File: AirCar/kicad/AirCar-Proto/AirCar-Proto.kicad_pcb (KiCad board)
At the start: 2 copper layers, 76.2 x 55.9 mm, 16 parts, among them J1 Conn_01x05, J3 Conn_01x06, J4 PJ-102A, SW2 SW_SPDT, U1 Pico, U2 LM7805_TO220

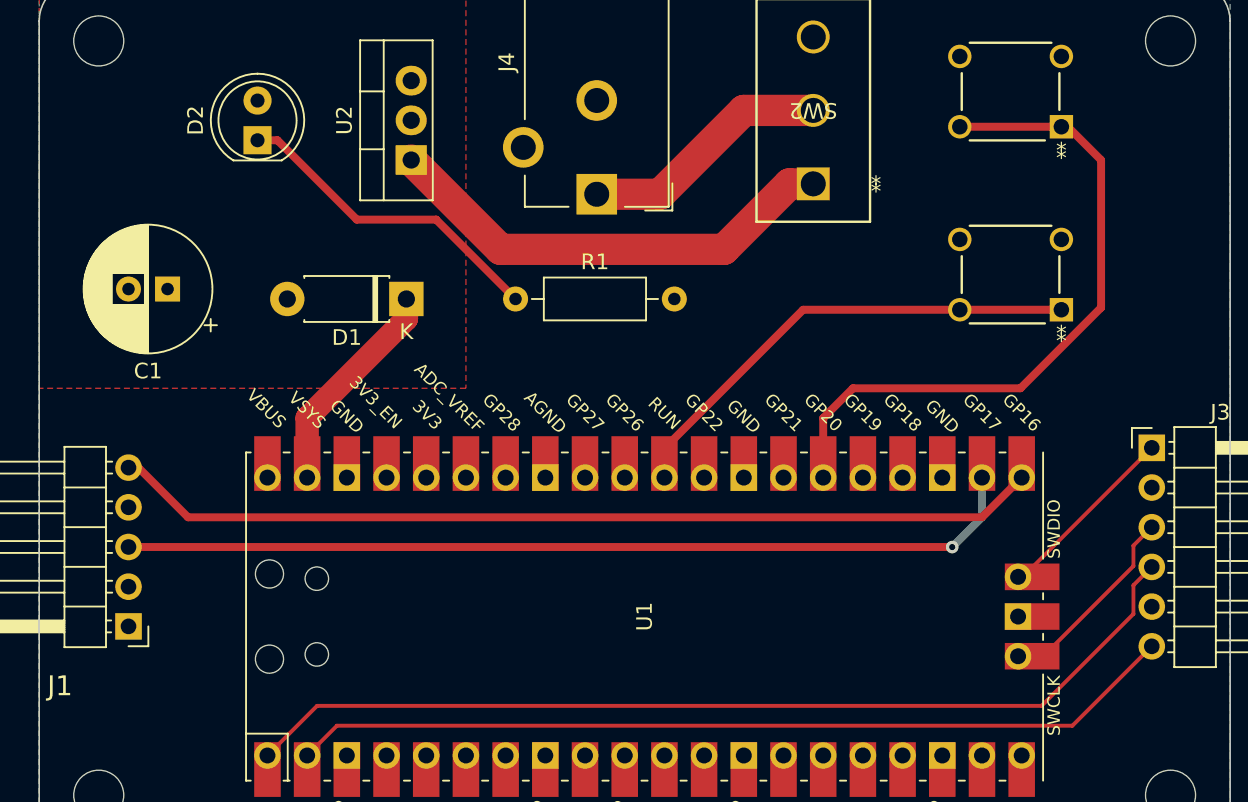
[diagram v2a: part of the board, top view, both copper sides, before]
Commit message: works w/ 3.3v encoder
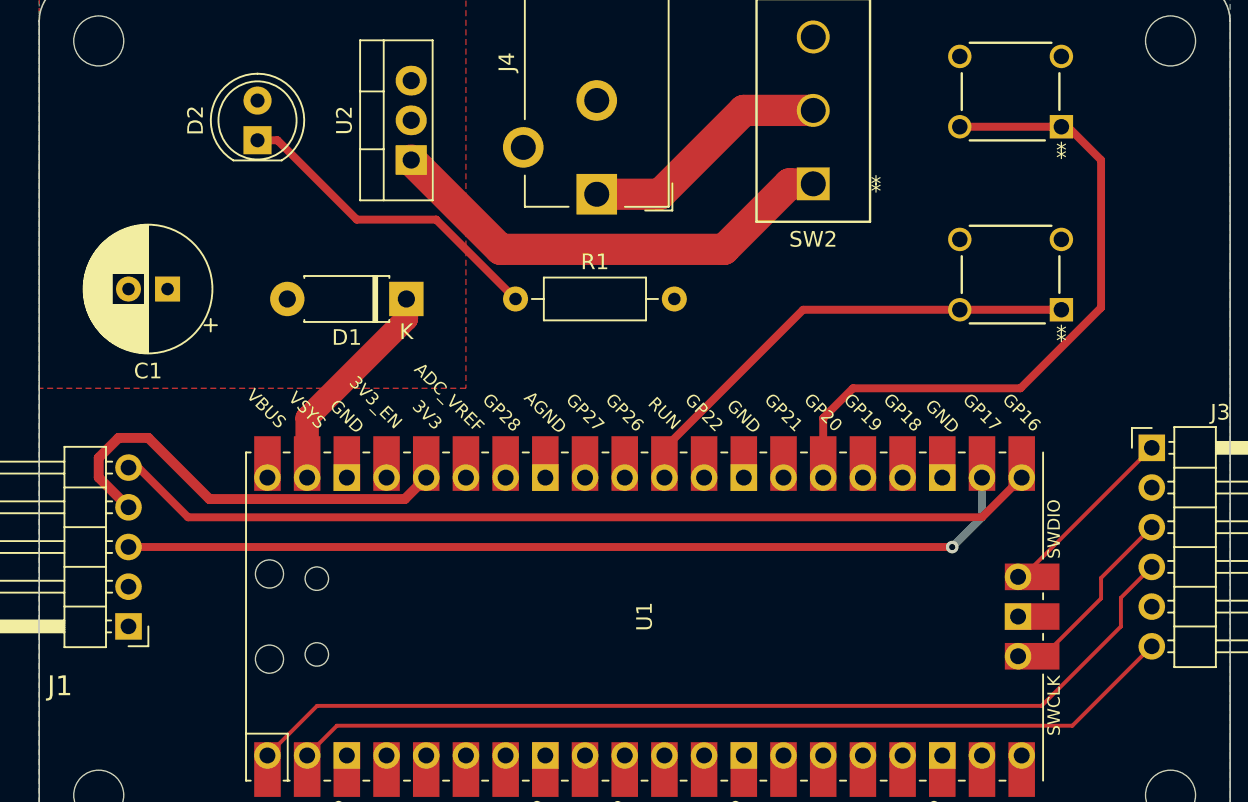
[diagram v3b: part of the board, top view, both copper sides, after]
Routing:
- net Net-(J1-Pin_4): track 0.00 -> 27.6 mm
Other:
- copper layers 2 -> 4
- board text removed: "Mounting Holes are for M3 posts."
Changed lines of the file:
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@@
   (layers
     (0 "F.Cu" signal)
+    (1 "In1.Cu" signal)
+    (2 "In2.Cu" signal)
     (31 "B.Cu" signal)
     (32 "B.Adhes" user "B.Adhesive")
@@
     (48 "B.Fab" user)
     (49 "F.Fab" user)
-    (50 "User.1" user)
-    (51 "User.2" user)
-    (52 "User.3" user)
-    (53 "User.4" user)
-    (54 "User.5" user)
-    (55 "User.6" user)
-    (56 "User.7" user)
-    (57 "User.8" user)
-    (58 "User.9" user)
   )
   (setup
@@
       (layer "F.SilkS" (type "Top Silk Screen"))
       (layer "F.Paste" (type "Top Solder Paste"))
-      (layer "F.Mask" (type "Top Solder Mask") (thickness 0.01))
+      (layer "F.Mask" (type "Top Solder Mask") (color "Green") (thickness 0.01))
       (layer "F.Cu" (type "copper") (thickness 0.035))
-      (layer "dielectric 1" (type "core") (thickness 1.51) (material "FR4") (epsilon_r 4.5) (loss_tangent 0.02))
+      (layer "dielectric 1" (type "prepreg") (thickness 0.1) (material "FR4") (epsilon_r 4.5) (loss_tangent 0.02))
+      (layer "In1.Cu" (type "copper") (thickness 0.035))
+      (layer "dielectric 2" (type "core") (thickness 1.24) (material "FR4") (epsilon_r 4.5) (loss_tangent 0.02))
+      (layer "In2.Cu" (type "copper") (thickness 0.035))
+      (layer "dielectric 3" (type "prepreg") (thickness 0.1) (material "FR4") (epsilon_r 4.5) (loss_tangent 0.02))
       (layer "B.Cu" (type "copper") (thickness 0.035))
-      (layer "B.Mask" (type "Bottom Solder Mask") (thickness 0.01))
+      (layer "B.Mask" (type "Bottom Solder Mask") (color "Green") (thickness 0.01))
       (layer "B.Paste" (type "Bottom Solder Paste"))
       (layer "B.SilkS" (type "Bottom Silk Screen"))
@@
     (pad "5" thru_hole oval (at 0 10.16 180) (size 1.7 1.7) (drill 1) (layers "*.Cu" "*.Mask")
       (net 20 "/Lag") (pinfunction "Pin_5") (pintype "passive"))
-    (model "${KICAD6_3DMODEL_DIR}/Connector_PinHeader_2.54mm.3dshapes/PinHeader_1x05_P2.54mm_Horizontal.wrl"
-      (offset (xyz 0 0 0))
+    (model "${KICAD6_3DMODEL_DIR}/Connector_PinHeader_2.54mm.3dshapes/PinHeader_1x05_P2.54mm_Horizontal.wrl" hide
+      (offset (xyz 0 3.175 0))
       (scale (xyz 1 1 1))
       (rotate (xyz 0 0 0))
+    )
+    (model "/Users/tad/Code/PiPico/AirCar/kicad/Library/705530004.stp"
+      (offset (xyz 7.112 -5.207 2.54))
+      (scale (xyz 1 1 1))
+      (rotate (xyz -90 0 -90))
     )
   )
@@
     (pad "4" thru_hole circle (at 0.000001 0 180) (size 1.4986 1.4986) (drill 0.9906) (layers "*.Cu" "*.Mask")
       (net 35 "GND") (pinfunction "4") (pintype "passive"))
+    (model "/Users/tad/Code/PiPico/AirCar/kicad/Library/c-1825910-6-c-3d.stp"
+      (offset (xyz -3.175 2.54 5.08))
+      (scale (xyz 1 1 1))
+      (rotate (xyz 0 0 90))
+    )
   )
   (footprint "Library:CS12ANW03_NKK" (layer "F.Cu")
@@
     (property "ki_keywords" "switch single-pole double-throw spdt ON-ON")
     (attr through_hole)
-    (fp_text reference "SW2" (at 0 4.699 180 unlocked) (layer "F.SilkS")
+    (fp_text reference "SW2" (at 0 -3.556 unlocked) (layer "F.SilkS")
         (effects (font (size 1 1) (thickness 0.15)))
     )
@@
     (pad "3" thru_hole circle (at 0 9.398 180) (size 2.1082 2.1082) (drill 1.6002) (layers "*.Cu" "*.Mask")
       (net 27 "unconnected-(SW2-C-Pad3)") (pinfunction "C") (pintype "passive+no_connect"))
+    (model "/Users/tad/Code/PiPico/AirCar/kicad/Library/CS12ANW03.stp"
+      (offset (xyz 0 -4.699 6.35))
+      (scale (xyz 1 1 1))
+      (rotate (xyz -90 0 0))
+    )
   )
   (footprint "Library:SW4_1825910-B_TEC" (layer "F.Cu")
@@
     (pad "4" thru_hole circle (at 0.000001 0 180) (size 1.4986 1.4986) (drill 0.9906) (layers "*.Cu" "*.Mask")
       (net 35 "GND") (pinfunction "4") (pintype "passive"))
+    (model "/Users/tad/Code/PiPico/AirCar/kicad/Library/c-1825910-6-c-3d.stp"
+      (offset (xyz -3.175 1.905 5.08))
+      (scale (xyz 1 1 1))
+      (rotate (xyz 0 0 90))
+    )
   )
   (footprint "Connector_BarrelJack:BarrelJack_CUI_PJ-102AH_Horizontal" (layer "F.Cu")
@@
     (pad "3" thru_hole circle (at 4.7 3 180) (size 2.6 2.6) (drill 1.6) (layers "*.Cu" "*.Mask")
       (net 35 "GND") (pintype "passive"))
-    (model "${KICAD6_3DMODEL_DIR}/Connector_BarrelJack.3dshapes/BarrelJack_CUI_PJ-102AH_Horizontal.wrl"
-      (offset (xyz 0 0 0))
+    (model "/Users/tad/Code/PiPico/AirCar/kicad/Library/CUI_DEVICES_PJ-102AH.step"
+      (offset (xyz 0 -13.97 6.35))
       (scale (xyz 1 1 1))
-      (rotate (xyz 0 0 0))
+      (rotate (xyz -90 0 90))
     )
   )
@@
   (gr_arc (start 66.04 157.48) (mid 64.243949 156.736051) (end 63.5 154.94)
     (stroke (width 0.1) (type default)) (layer "Edge.Cuts"))
-  (gr_text "Mounting Holes are for M3 posts." (at 80.01 160.655) (layer "User.2")
-    (effects (font (size 2.032 2.032) (thickness 0.254)) (justify left bottom))
-  )
-  (dimension (type aligned) (layer "User.1")
-    (pts (xy 63.5 140.97) (xy 139.7 140.97))
-    (height 34.29)
-    (gr_text "76.2000 mm" (at 101.6 174.11) (layer "User.1")
-      (effects (font (size 1 1) (thickness 0.15)))
-    )
-    (format (prefix "") (suffix "") (units 3) (units_format 1) (precision 4))
-    (style (thickness 0.1) (arrow_length 1.27) (text_position_mode 0) (extension_height 0.58642) (extension_offset 0.5) keep_text_aligned)
-  )
-  (dimension (type aligned) (layer "User.1")
-    (pts (xy 135.89 105.41) (xy 135.89 153.67))
-    (height -13.97)
-    (gr_text "48.2600 mm" (at 148.71 129.54 90) (layer "User.1")
-      (effects (font (size 1 1) (thickness 0.15)))
-    )
-    (format (prefix "") (suffix "") (units 3) (units_format 1) (precision 4))
-    (style (thickness 0.1) (arrow_length 1.27) (text_position_mode 0) (extension_height 0.58642) (extension_offset 0.5) keep_text_aligned)
-  )
-  (dimension (type aligned) (layer "User.1")
-    (pts (xy 119.38 101.6) (xy 119.38 157.48))
-    (height -40.64)
-    (gr_text "55.8800 mm" (at 158.87 129.54 90) (layer "User.1")
-      (effects (font (size 1 1) (thickness 0.15)))
-    )
-    (format (prefix "") (suffix "") (units 3) (units_format 1) (precision 4))
-    (style (thickness 0.1) (arrow_length 1.27) (text_position_mode 0) (extension_height 0.58642) (extension_offset 0.5) keep_text_aligned)
-  )
-  (dimension (type aligned) (layer "User.1")
-    (pts (xy 63.5 112.395) (xy 99.06 112.395))
-    (height -19.05)
-    (gr_text "35.5600 mm" (at 81.28 92.195) (layer "User.1")
-      (effects (font (size 1 1) (thickness 0.15)))
-    )
-    (format (prefix "") (suffix "") (units 3) (units_format 1) (precision 4))
-    (style (thickness 0.1) (arrow_length 1.27) (text_position_mode 0) (extension_height 0.58642) (extension_offset 0.5) keep_text_aligned)
-  )
-  (dimension (type aligned) (layer "User.1")
-    (pts (xy 67.31 153.67) (xy 135.89 153.67))
-    (height 13.969999)
-    (gr_text "68.5800 mm" (at 101.6 166.489999) (layer "User.1")
-      (effects (font (size 1 1) (thickness 0.15)))
-    )
-    (format (prefix "") (suffix "") (units 3) (units_format 1) (precision 4))
-    (style (thickness 0.1) (arrow_length 1.27) (text_position_mode 0) (extension_height 0.58642) (extension_offset 0.5) keep_text_aligned)
-  )
-  (segment (start 133.515 140.24) (end 134.69 139.065) (width 0.25) (layer "F.Cu") (net 1))
-  (segment (start 133.515 142.075) (end 133.515 140.24) (width 0.25) (layer "F.Cu") (net 1))
+  (segment (start 78.105 151.13) (end 81.28 147.955) (width 0.25) (layer "F.Cu") (net 1))
+  (segment (start 127.635 147.955) (end 132.715 142.875) (width 0.25) (layer "F.Cu") (net 1))
   (segment (start 81.28 147.955) (end 127.635 147.955) (width 0.25) (layer "F.Cu") (net 1))
-  (segment (start 78.105 151.13) (end 81.28 147.955) (width 0.25) (layer "F.Cu") (net 1))
-  (segment (start 127.635 147.955) (end 133.515 142.075) (width 0.25) (layer "F.Cu") (net 1))
+  (segment (start 132.715 141.04) (end 134.69 139.065) (width 0.25) (layer "F.Cu") (net 1))
+  (segment (start 132.715 142.875) (end 132.715 141.04) (width 0.25) (layer "F.Cu") (net 1))
   (segment (start 129.61 149.225) (end 134.69 144.145) (width 0.25) (layer "F.Cu") (net 2))
   (segment (start 82.55 149.225) (end 129.61 149.225) (width 0.25) (layer "F.Cu") (net 2))
@@
   (segment (start 99.175 115.22) (end 103.22 115.22) (width 2) (layer "F.Cu") (net 25))
   (segment (start 103.22 115.22) (end 108.585 109.855) (width 2) (layer "F.Cu") (net 25))
-  (segment (start 133.515 139.01) (end 127.745 144.78) (width 0.25) (layer "F.Cu") (net 37))
+  (segment (start 74.3957 134.7207) (end 86.8943 134.7207) (width 0.635) (layer "F.Cu") (net 33))
+  (segment (start 86.8943 134.7207) (end 88.265 133.35) (width 0.635) (layer "F.Cu") (net 33))
+  (segment (start 67.31 132.08) (end 68.58 130.81) (width 0.635) (layer "F.Cu") (net 33))
+  (segment (start 69.215 135.25) (end 67.31 133.345) (width 0.635) (layer "F.Cu") (net 33))
+  (segment (start 67.31 133.345) (end 67.31 132.08) (width 0.635) (layer "F.Cu") (net 33))
+  (segment (start 70.485 130.81) (end 74.3957 134.7207) (width 0.635) (layer "F.Cu") (net 33))
+  (segment (start 68.58 130.81) (end 70.485 130.81) (width 0.635) (layer "F.Cu") (net 33))
+  (segment (start 131.445 139.77) (end 131.445 141.08) (width 0.25) (layer "F.Cu") (net 37))
   (segment (start 127.745 144.78) (end 126.135 144.78) (width 0.25) (layer "F.Cu") (net 37))
-  (segment (start 134.69 136.525) (end 133.515 137.7) (width 0.25) (layer "F.Cu") (net 37))
-  (segment (start 133.515 137.7) (end 133.515 139.01) (width 0.25) (layer "F.Cu") (net 37))
+  (segment (start 131.445 141.08) (end 127.745 144.78) (width 0.25) (layer "F.Cu") (net 37))
+  (segment (start 134.69 136.525) (end 131.445 139.77) (width 0.25) (layer "F.Cu") (net 37))
   (segment (start 126.135 139.7) (end 126.435 139.7) (width 0.25) (layer "F.Cu") (net 38))
   (segment (start 126.435 139.7) (end 134.69 131.445) (width 0.25) (layer "F.Cu") (net 38))

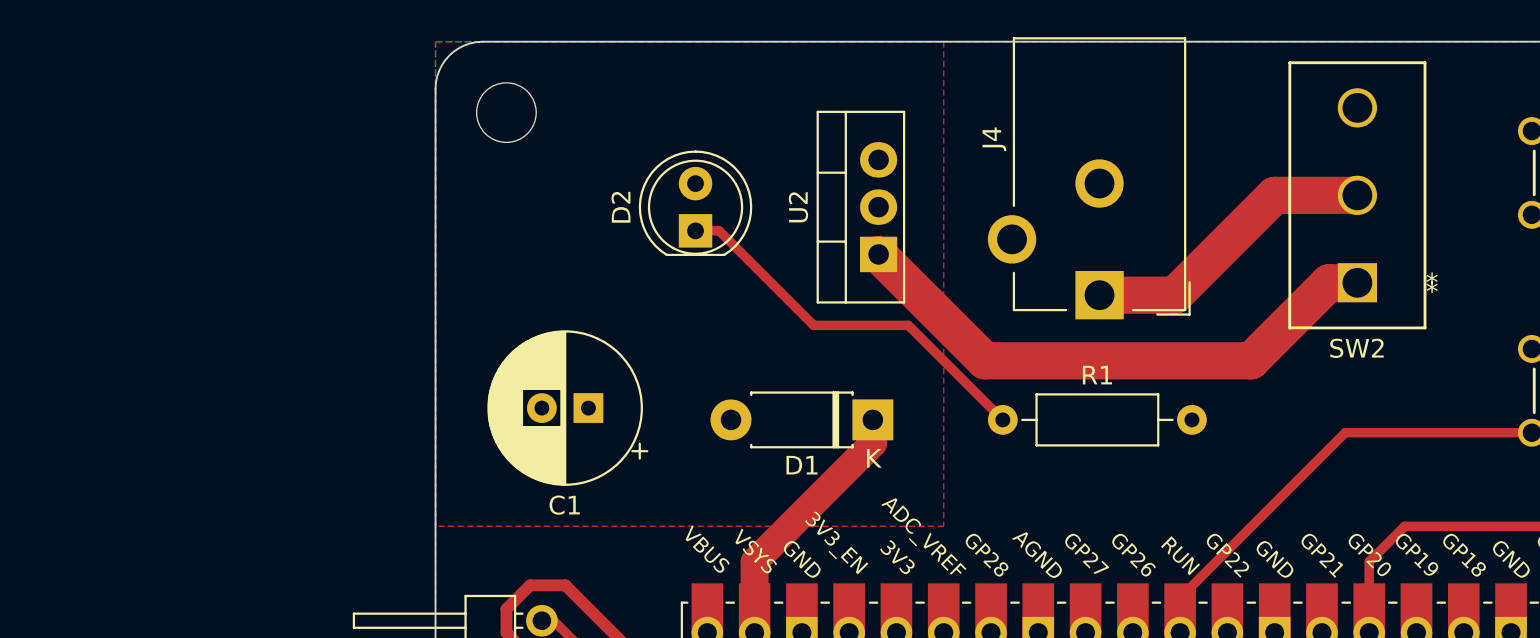
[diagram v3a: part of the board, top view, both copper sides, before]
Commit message: work on adding level shifter
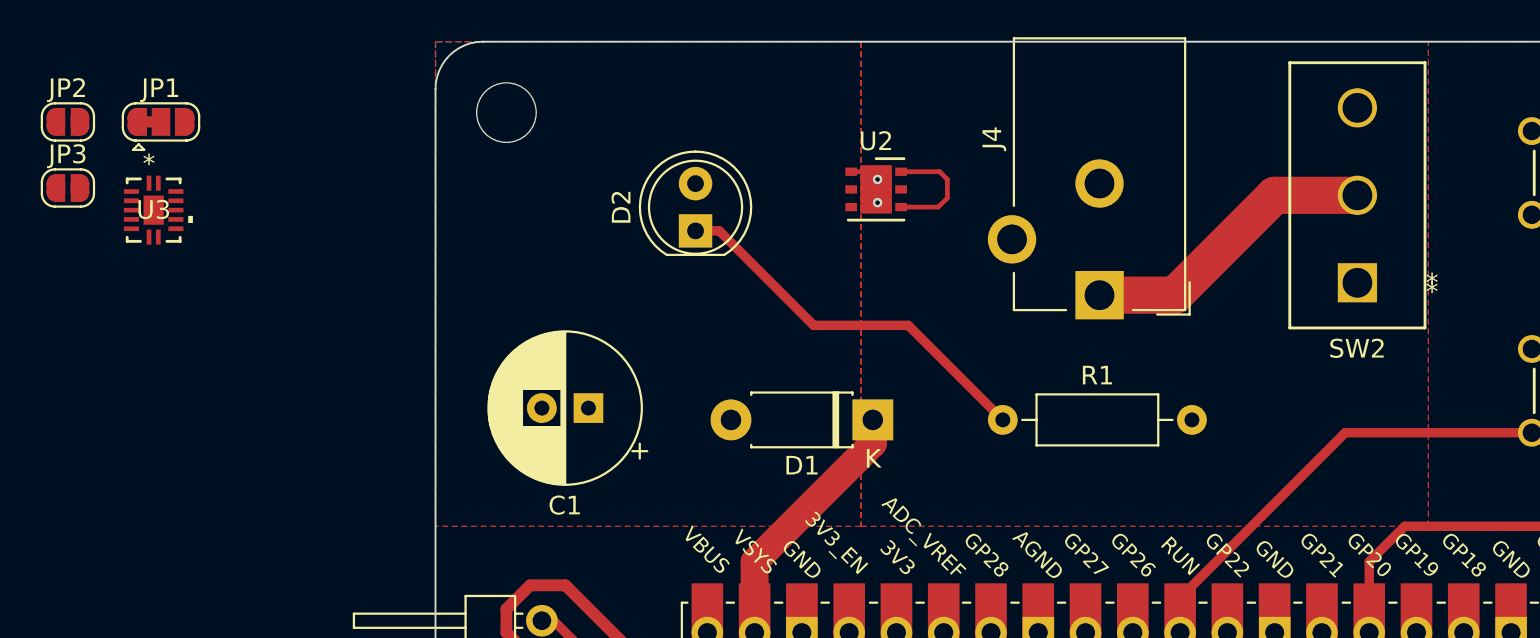
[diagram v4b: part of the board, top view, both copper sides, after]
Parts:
- added JP1: SolderJumper_3_Bridged12, Jumper:SolderJumper-3_P1.3mm_Bridged12_RoundedPad1.0x1.5mm, F.Cu at (48.8, 105.9)
- added JP2: SolderJumper_2_Open, Jumper:SolderJumper-2_P1.3mm_Open_RoundedPad1.0x1.5mm, F.Cu at (43.8, 105.9)
- added JP3: SolderJumper_2_Open, Jumper:SolderJumper-2_P1.3mm_Open_RoundedPad1.0x1.5mm, F.Cu at (43.8, 109.5)
- added U3: TXU0104BQAR, Library:U_TXU0104_TEX, F.Cu at (48.4, 110.6)
- U2: value LM7805_TO220 -> LDL212PU50R; footprint Package_TO_SOT_THT:TO-220-3_Vertical -> Package_DFN_QFN:DFN-6-1EP_3x3mm_P0.95mm_EP1.7x2.6mm
- moved U2 3.50 mm to (87.2, 109.5), turned to 0 degrees
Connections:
- J1 pad 4: Net-(J1-Pin_4) -> /Venc
- U1 pad 21: /Lag -> /Lag_3P3
- U1 pad 22: /Lead -> /Lead_3P3
- U1 pad 36: Net-(J1-Pin_4) -> /V3P3
- U2 pad 1: /V9P0_SW -> GND
- U2 pad 2: GND -> /V5p0
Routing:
- net Net-(J1-Pin_4): track 27.6 -> 0.00 mm
- net (no net): track 0.00 -> 27.6 mm
- net /V9P0_SW: track 29.8 -> 6.13 mm
- net GND: track 0.00 -> 2.92 mm, vias 0 -> 2
- added copper zone on F.Cu, net /V9P0_SW

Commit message: wip
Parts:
- added J2: Conn_01x20_Socket, Connector_PinHeader_2.54mm:PinHeader_1x20_P2.54mm_Vertical, F.Cu at (78.1, 133.3)
- added J5: Conn_01x20_Socket, Connector_PinHeader_2.54mm:PinHeader_1x20_P2.54mm_Vertical, F.Cu at (126.4, 151.1)
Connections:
- U1 pad 10: unconnected-(U1-GPIO7-Pad10) -> Net-(J5-Pin_11)
- U1 pad 11: unconnected-(U1-GPIO8-Pad11) -> Net-(J5-Pin_10)
- U1 pad 12: unconnected-(U1-GPIO9-Pad12) -> Net-(J5-Pin_9)
- U1 pad 13: unconnected-(U1-GND-Pad13) -> GND
- U1 pad 14: unconnected-(U1-GPIO10-Pad14) -> Net-(J5-Pin_7)
- U1 pad 15: unconnected-(U1-GPIO11-Pad15) -> Net-(J5-Pin_6)
- U1 pad 16: unconnected-(U1-GPIO12-Pad16) -> Net-(J5-Pin_5)
- U1 pad 17: unconnected-(U1-GPIO13-Pad17) -> Net-(J5-Pin_4)
- U1 pad 19: unconnected-(U1-GPIO14-Pad19) -> Net-(J5-Pin_2)
- U1 pad 20: unconnected-(U1-GPIO15-Pad20) -> Net-(J5-Pin_1)
- U1 pad 24: unconnected-(U1-GPIO18-Pad24) -> Net-(J2-Pin_17)
- U1 pad 25: unconnected-(U1-GPIO19-Pad25) -> Net-(J2-Pin_16)
- U1 pad 27: unconnected-(U1-GPIO21-Pad27) -> Net-(J2-Pin_14)
- U1 pad 29: unconnected-(U1-GPIO22-Pad29) -> Net-(J2-Pin_12)
- U1 pad 31: unconnected-(U1-GPIO26_ADC0-Pad31) -> Net-(J2-Pin_10)
- U1 pad 32: unconnected-(U1-GPIO27_ADC1-Pad32) -> Net-(J2-Pin_9)
- U1 pad 34: unconnected-(U1-GPIO28_ADC2-Pad34) -> Net-(J2-Pin_7)
- U1 pad 35: unconnected-(U1-ADC_VREF-Pad35) -> Net-(J2-Pin_6)
- U1 pad 37: unconnected-(U1-3V3_EN-Pad37) -> Net-(J2-Pin_4)
- U1 pad 4: unconnected-(U1-GPIO2-Pad4) -> Net-(J5-Pin_17)
- U1 pad 40: unconnected-(U1-VBUS-Pad40) -> Net-(J2-Pin_1)
- U1 pad 5: unconnected-(U1-GPIO3-Pad5) -> Net-(J5-Pin_16)
- U1 pad 6: unconnected-(U1-GPIO4-Pad6) -> Net-(J5-Pin_15)
- U1 pad 7: unconnected-(U1-GPIO5-Pad7) -> Net-(J5-Pin_14)
- U1 pad 9: unconnected-(U1-GPIO6-Pad9) -> Net-(J5-Pin_12)
